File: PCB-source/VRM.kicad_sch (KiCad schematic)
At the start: 2 parts, among them U1 LMR516x5, U2 LMR516x5

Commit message: vrm VIP
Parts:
- removed U1, U2: LMR516x5, Package_TO_SOT_SMD:SOT-23-6, symbol LMR51625:LMR51625
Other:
- added sheet LMR74700-1 (LMR74700.kicad_sch)
- added sheet LMR74700-2 (LMR74700.kicad_sch)
- added sheet LMR74700-3 (LMR74700.kicad_sch)
- added sheet SIC471 (SIC471.kicad_sch)
- added sheet TPS563200-1 (TPS563200.kicad_sch)
- added sheet TPS563200-2 (TPS563200.kicad_sch)
- note added: "55V MAX!"
- note removed: "DONT FORGET TO ADD TVS ON VIN!!!"

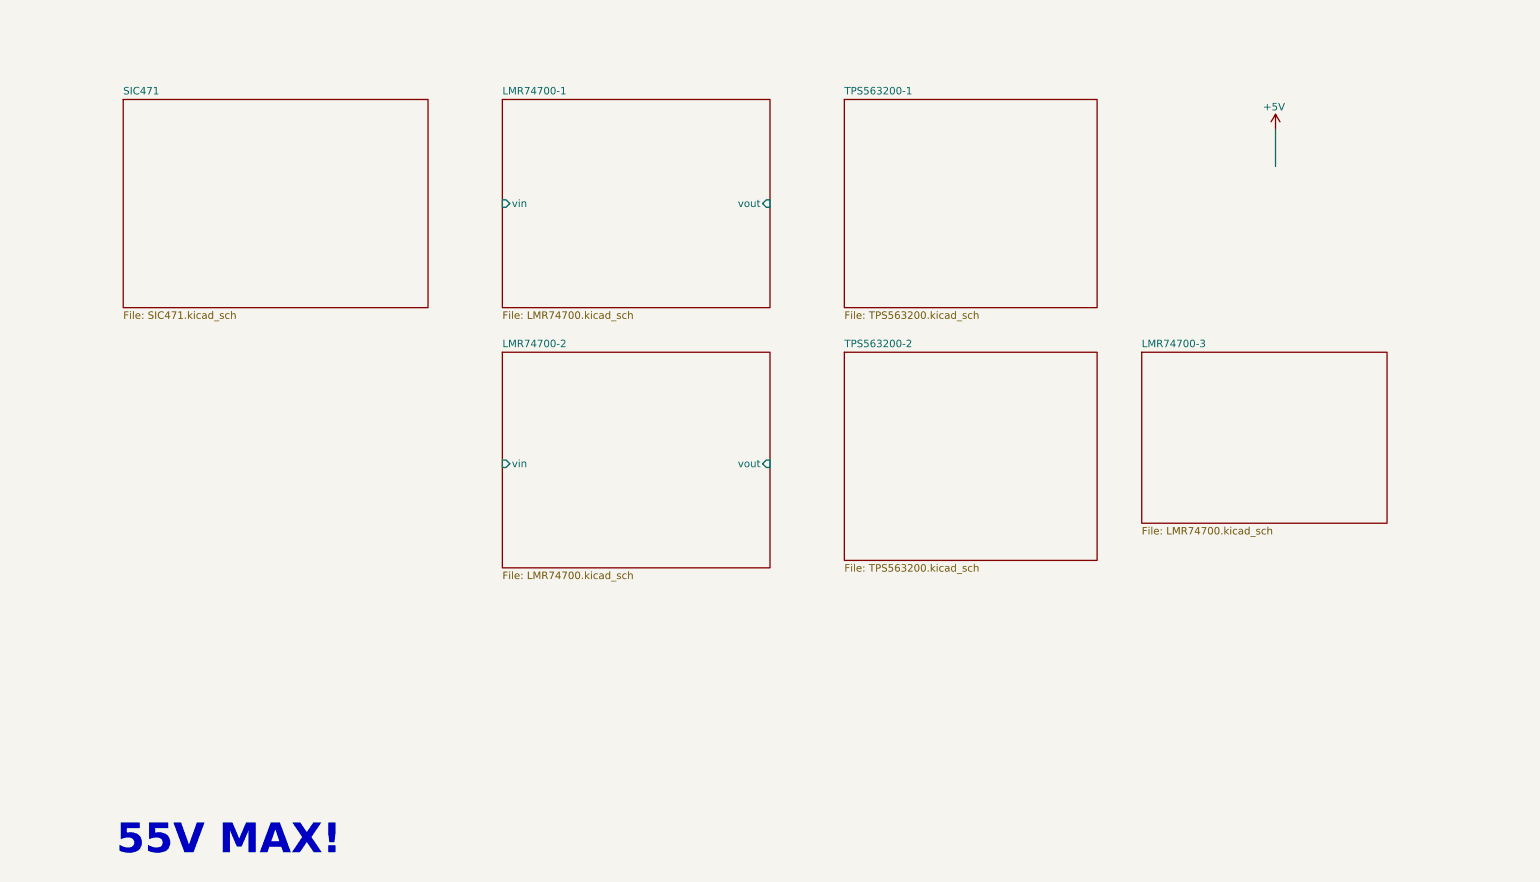
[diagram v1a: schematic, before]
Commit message: Finish component and diffpair placement
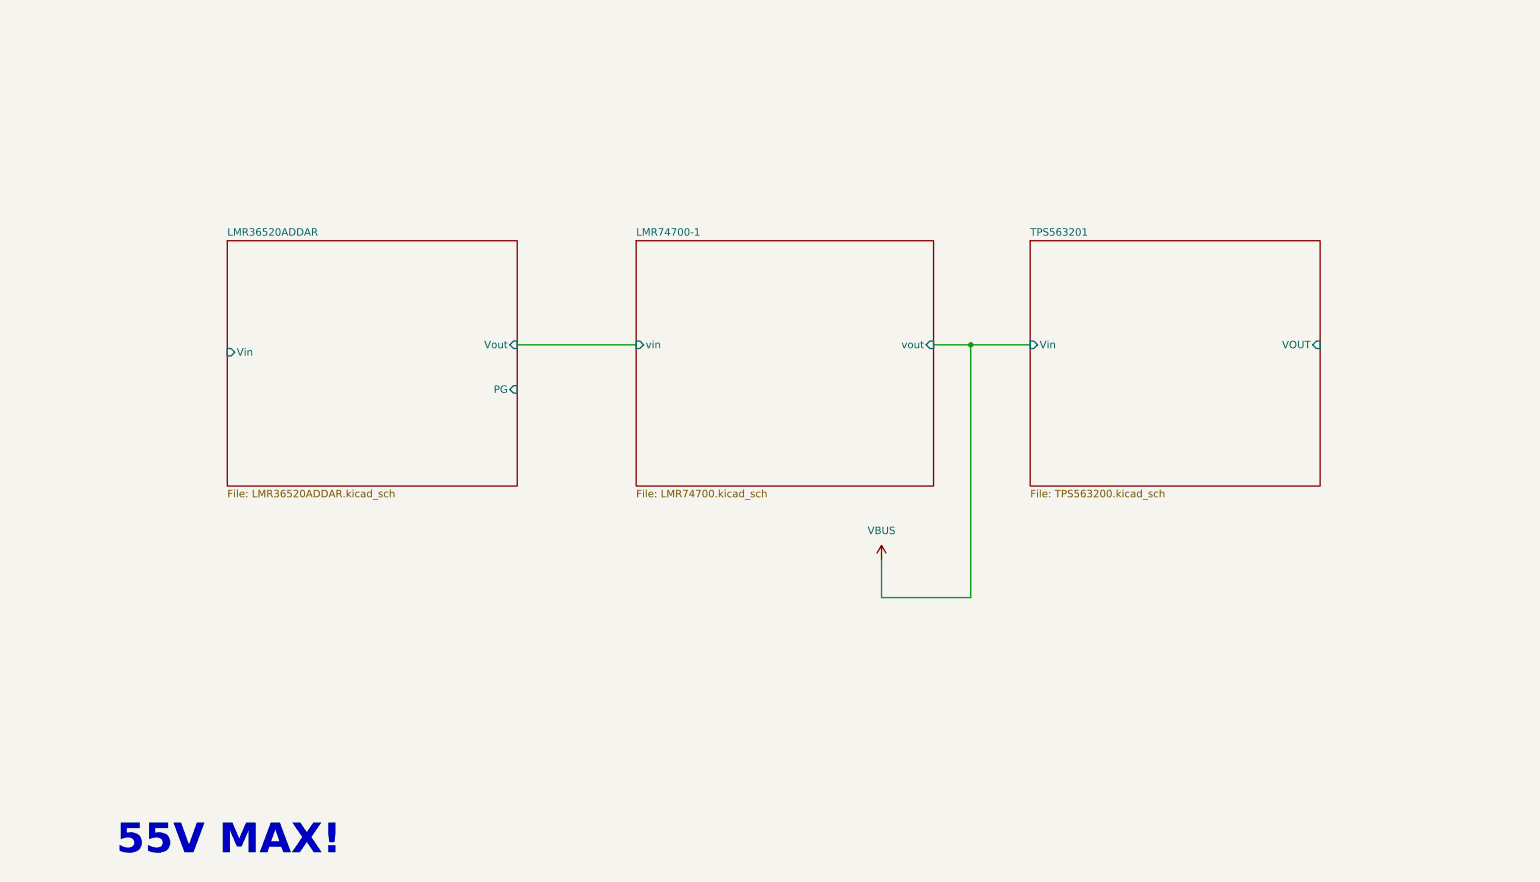
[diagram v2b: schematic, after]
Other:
- sheet TPS563200-1 renamed TPS563201
- removed sheet LMR74700-2
- removed sheet LMR74700-3
- removed sheet SIC471
- removed sheet TPS563200-2
- added sheet LMR36520ADDAR (LMR36520ADDAR.kicad_sch)
- sheet TPS563201 ports: added VOUT, Vin; removed none
- title: MMS2 -> MMS2 VRM

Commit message: in progress
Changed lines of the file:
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@@
 	(wire
 		(pts
+			(xy 54.61 88.9) (xy 40.64 88.9)
+		)
+		(stroke
+			(width 0)
+			(type default)
+		)
+	)
+	(wire
+		(pts
 			(xy 166.37 130.81) (xy 181.61 130.81)
 		)
@@
 	(wire
 		(pts
+			(xy 40.64 81.28) (xy 40.64 88.9)
+		)
+		(stroke
+			(width 0)
+			(type default)
+		)
+	)
+	(wire
+		(pts
 			(xy 175.26 87.63) (xy 181.61 87.63)
 		)
@@
 		)
 	)
+	(symbol
+		(lib_id "power:VCC")
+		(at 40.64 81.28 0)
+		(unit 1)
+		(exclude_from_sim no)
+		(in_bom yes)
+		(on_board yes)
+		(dnp no)
+		(fields_autoplaced yes)
+		(property "Reference" "#PWR026"
+			(at 40.64 85.09 0)
+			(effects
+				(font
+					(size 1.27 1.27)
+				)
+				(hide yes)
+			)
+		)
+		(property "Value" "BRD_VIN"
+			(at 40.64 76.2 0)
+			(effects
+				(font
+					(size 1.27 1.27)
+				)
+			)
+		)
+		(property "Footprint" ""
+			(at 40.64 81.28 0)
+			(effects
+				(font
+					(size 1.27 1.27)
+				)
+				(hide yes)
+			)
+		)
+		(property "Datasheet" ""
+			(at 40.64 81.28 0)
+			(effects
+				(font
+					(size 1.27 1.27)
+				)
+				(hide yes)
+			)
+		)
+		(property "Description" "Power symbol creates a global label with name \"VCC\""
+			(at 40.64 81.28 0)
+			(effects
+				(font
+					(size 1.27 1.27)
+				)
+				(hide yes)
+			)
+		)
+		(pin "1"
+		)
+		(instances
+			(project "MMS2"
+				(path "/6596548a-44e0-46d8-8624-fd71cf4a3e17/c3406df1-7cb0-4484-a477-0c72b46ba076"
+					(reference "#PWR026")
+					(unit 1)
+				)
+			)
+		)
+	)
